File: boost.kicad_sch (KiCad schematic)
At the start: 24 parts, among them Q13 BSC059N04LS6, Q8 BSC059N04LS6, U7 LM5123-Q1

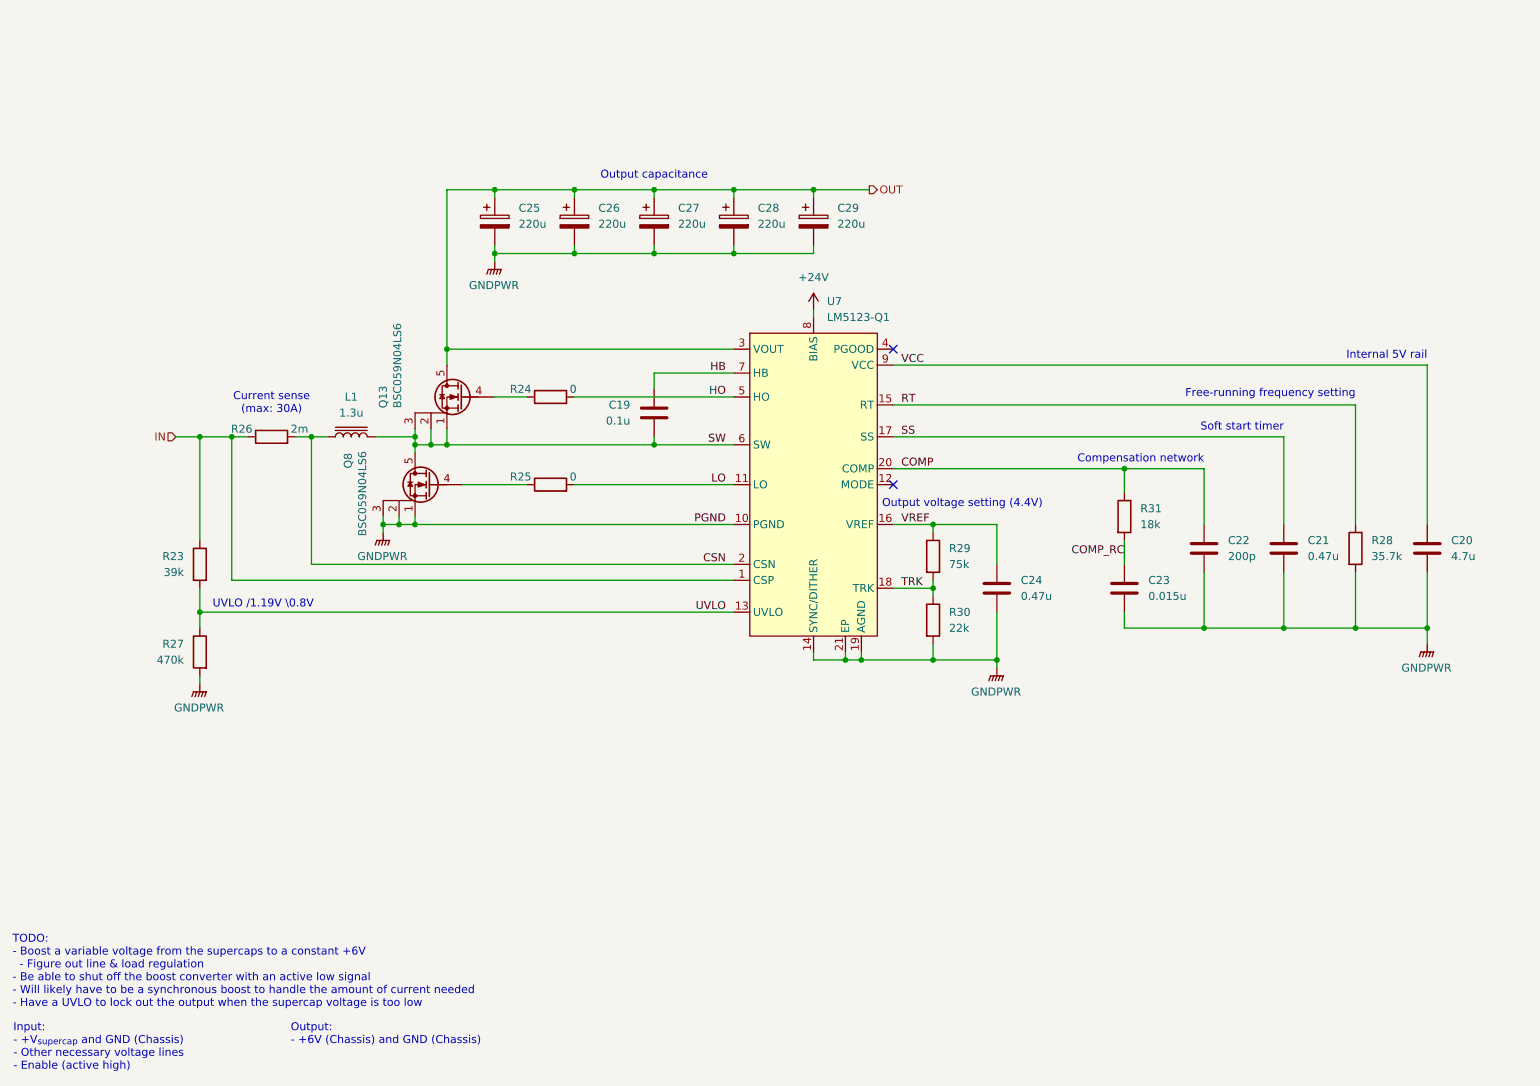
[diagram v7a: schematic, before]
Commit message: Reannotate schematic
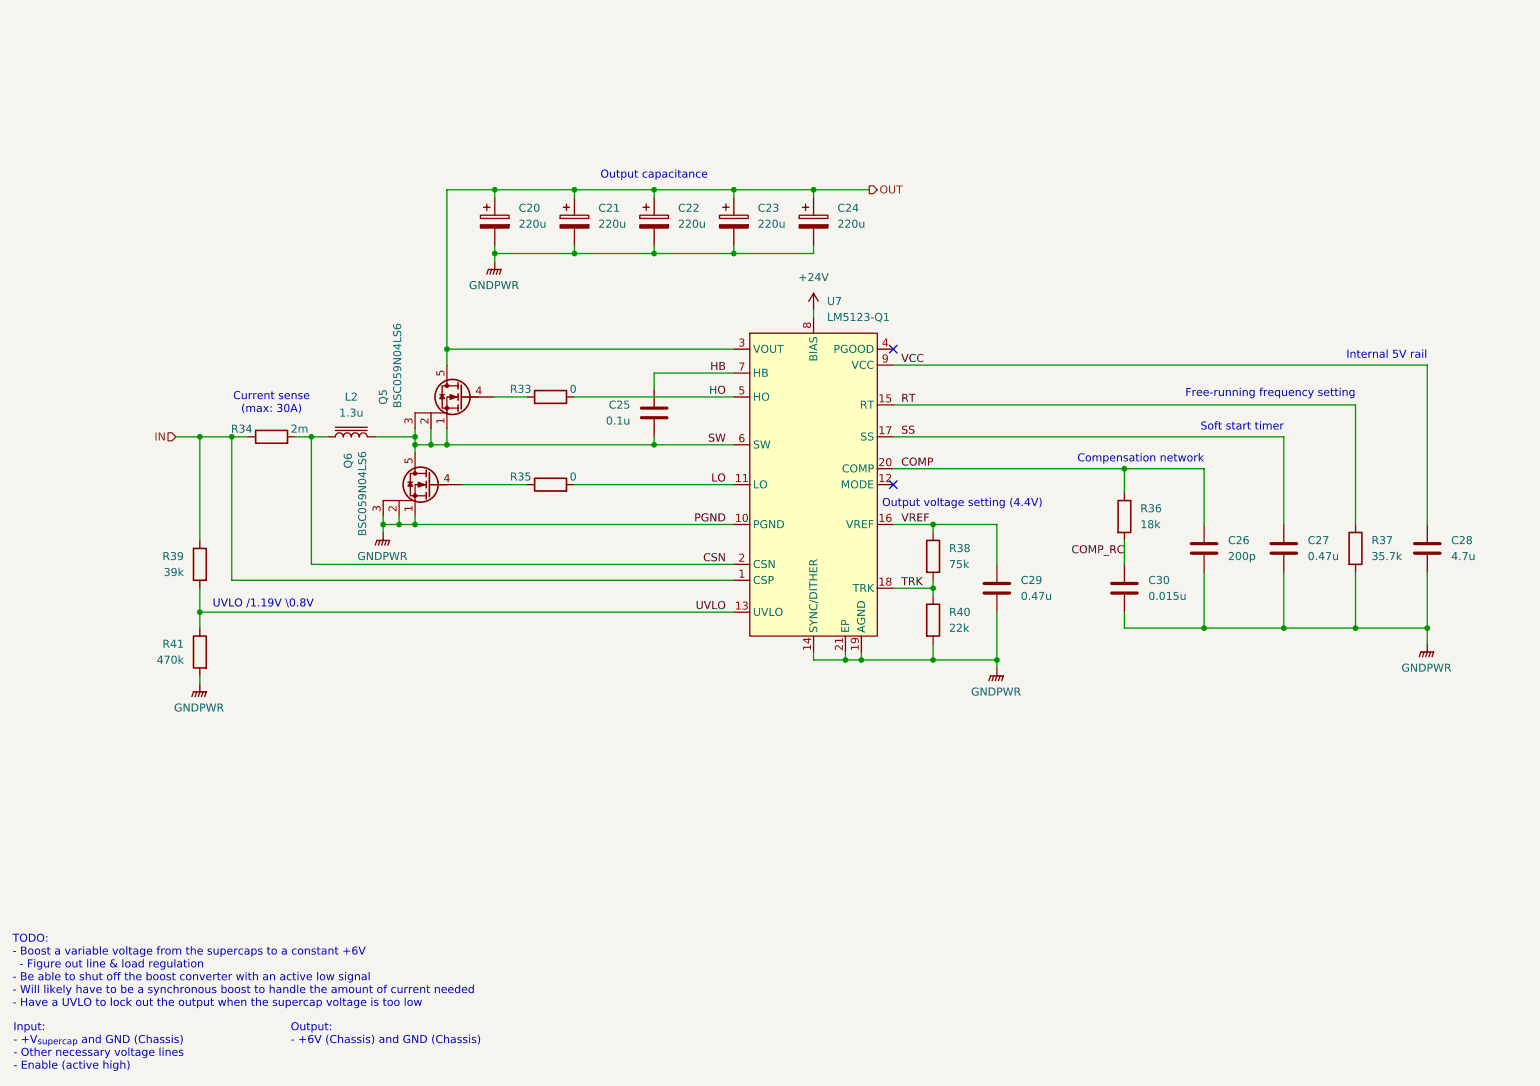
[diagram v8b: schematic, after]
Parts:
- renumbered C25 to C20, C26 to C21, C27 to C22, C28 to C23, C29 to C24, C19 to C25, C22 to C26, C21 to C27, C20 to C28, C24 to C29, C23 to C30, L1 to L2, Q13 to Q5, Q8 to Q6, R24 to R33, R26 to R34, R25 to R35, R31 to R36, R28 to R37, R29 to R38, R23 to R39, R30 to R40, R27 to R41
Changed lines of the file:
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@@
 		(on_board yes)
 		(dnp no)
-		(property "Reference" "Q13"
+		(property "Reference" "Q5"
 			(at 78.74 83.82 90)
 			(effects
@@
 			(project "SupercapManager"
 				(path "/6197145b-e7d4-44cc-9d90-537b6501bf60/fd749e99-bd1e-4aca-86d6-8b572dc00b7d"
-					(reference "Q13")
+					(reference "Q5")
 					(unit 1)
 				)
@@
 		(on_board yes)
 		(dnp no)
-		(property "Reference" "R27"
+		(property "Reference" "R41"
 			(at 46.99 123.1899 0)
 			(effects
@@
 			(project "SupercapManager"
 				(path "/6197145b-e7d4-44cc-9d90-537b6501bf60/fd749e99-bd1e-4aca-86d6-8b572dc00b7d"
-					(reference "R27")
+					(reference "R41")
 					(unit 1)
 				)
@@
 		(dnp no)
 		(fields_autoplaced yes)
-		(property "Reference" "C27"
+		(property "Reference" "C22"
 			(at 125.73 53.7209 0)
 			(effects
@@
 			(project "SupercapManager"
 				(path "/6197145b-e7d4-44cc-9d90-537b6501bf60/fd749e99-bd1e-4aca-86d6-8b572dc00b7d"
-					(reference "C27")
+					(reference "C22")
 					(unit 1)
 				)
@@
 		(dnp no)
 		(fields_autoplaced yes)
-		(property "Reference" "#PWR046"
+		(property "Reference" "#PWR050"
 			(at 245.11 128.27 0)
 			(effects
@@
 			(project "SupercapManager"
 				(path "/6197145b-e7d4-44cc-9d90-537b6501bf60/fd749e99-bd1e-4aca-86d6-8b572dc00b7d"
-					(reference "#PWR046")
+					(reference "#PWR050")
 					(unit 1)
 				)
@@
 		(on_board yes)
 		(dnp no)
-		(property "Reference" "C20"
+		(property "Reference" "C28"
 			(at 248.92 106.6799 0)
 			(effects
@@
 			(project "SupercapManager"
 				(path "/6197145b-e7d4-44cc-9d90-537b6501bf60/fd749e99-bd1e-4aca-86d6-8b572dc00b7d"
-					(reference "C20")
+					(reference "C28")
 					(unit 1)
 				)
@@
 		(dnp no)
 		(fields_autoplaced yes)
-		(property "Reference" "C25"
+		(property "Reference" "C20"
 			(at 100.33 53.7209 0)
 			(effects
@@
 			(project ""
 				(path "/6197145b-e7d4-44cc-9d90-537b6501bf60/fd749e99-bd1e-4aca-86d6-8b572dc00b7d"
-					(reference "C25")
+					(reference "C20")
 					(unit 1)
 				)
@@
 		(dnp no)
 		(fields_autoplaced yes)
-		(property "Reference" "#PWR020"
+		(property "Reference" "#PWR051"
 			(at 176.53 132.08 0)
 			(effects
@@
 			(project ""
 				(path "/6197145b-e7d4-44cc-9d90-537b6501bf60/fd749e99-bd1e-4aca-86d6-8b572dc00b7d"
-					(reference "#PWR020")
+					(reference "#PWR051")
 					(unit 1)
 				)
@@
 		(on_board yes)
 		(dnp no)
-		(property "Reference" "R28"
+		(property "Reference" "R37"
 			(at 236.22 106.6799 0)
 			(effects
@@
 			(project "SupercapManager"
 				(path "/6197145b-e7d4-44cc-9d90-537b6501bf60/fd749e99-bd1e-4aca-86d6-8b572dc00b7d"
-					(reference "R28")
+					(reference "R37")
 					(unit 1)
 				)
@@
 		(on_board yes)
 		(dnp no)
-		(property "Reference" "C22"
+		(property "Reference" "C26"
 			(at 213.36 106.6799 0)
 			(effects
@@
 			(project "SupercapManager"
 				(path "/6197145b-e7d4-44cc-9d90-537b6501bf60/fd749e99-bd1e-4aca-86d6-8b572dc00b7d"
-					(reference "C22")
+					(reference "C26")
 					(unit 1)
 				)
@@
 		(on_board yes)
 		(dnp no)
-		(property "Reference" "R23"
+		(property "Reference" "R39"
 			(at 46.99 109.2199 0)
 			(effects
@@
 			(project ""
 				(path "/6197145b-e7d4-44cc-9d90-537b6501bf60/fd749e99-bd1e-4aca-86d6-8b572dc00b7d"
-					(reference "R23")
+					(reference "R39")
 					(unit 1)
 				)
@@
 		(on_board yes)
 		(dnp no)
-		(property "Reference" "R24"
+		(property "Reference" "R33"
 			(at 102.362 83.312 90)
 			(effects
@@
 			(project "SupercapManager"
 				(path "/6197145b-e7d4-44cc-9d90-537b6501bf60/fd749e99-bd1e-4aca-86d6-8b572dc00b7d"
-					(reference "R24")
+					(reference "R33")
 					(unit 1)
 				)
@@
 		(on_board yes)
 		(dnp no)
-		(property "Reference" "R25"
+		(property "Reference" "R35"
 			(at 102.362 97.282 90)
 			(effects
@@
 			(project "SupercapManager"
 				(path "/6197145b-e7d4-44cc-9d90-537b6501bf60/fd749e99-bd1e-4aca-86d6-8b572dc00b7d"
-					(reference "R25")
+					(reference "R35")
 					(unit 1)
 				)
@@
 		(dnp no)
 		(fields_autoplaced yes)
-		(property "Reference" "C29"
+		(property "Reference" "C24"
 			(at 151.13 53.7209 0)
 			(effects
@@
 			(project "SupercapManager"
 				(path "/6197145b-e7d4-44cc-9d90-537b6501bf60/fd749e99-bd1e-4aca-86d6-8b572dc00b7d"
-					(reference "C29")
+					(reference "C24")
 					(unit 1)
 				)
@@
 		(on_board yes)
 		(dnp no)
-		(property "Reference" "R26"
+		(property "Reference" "R34"
 			(at 57.912 89.662 90)
 			(effects
@@
 			(project "SupercapManager"
 				(path "/6197145b-e7d4-44cc-9d90-537b6501bf60/fd749e99-bd1e-4aca-86d6-8b572dc00b7d"
-					(reference "R26")
+					(reference "R34")
 					(unit 1)
 				)
@@
 		(on_board yes)
 		(dnp no)
-		(property "Reference" "C21"
+		(property "Reference" "C27"
 			(at 226.06 106.6799 0)
 			(effects
@@
 			(project "SupercapManager"
 				(path "/6197145b-e7d4-44cc-9d90-537b6501bf60/fd749e99-bd1e-4aca-86d6-8b572dc00b7d"
-					(reference "C21")
+					(reference "C27")
 					(unit 1)
 				)
@@
 		(on_board yes)
 		(dnp no)
-		(property "Reference" "C23"
+		(property "Reference" "C30"
 			(at 200.66 113.0299 0)
 			(effects
@@
 			(project "SupercapManager"
 				(path "/6197145b-e7d4-44cc-9d90-537b6501bf60/fd749e99-bd1e-4aca-86d6-8b572dc00b7d"
-					(reference "C23")
+					(reference "C30")
 					(unit 1)
 				)
@@
 		(on_board yes)
 		(dnp no)
-		(property "Reference" "R30"
+		(property "Reference" "R40"
 			(at 168.91 118.1099 0)
 			(effects
@@
 			(project "SupercapManager"
 				(path "/6197145b-e7d4-44cc-9d90-537b6501bf60/fd749e99-bd1e-4aca-86d6-8b572dc00b7d"
-					(reference "R30")
+					(reference "R40")
 					(unit 1)
 				)
@@
 		(dnp no)
 		(fields_autoplaced yes)
-		(property "Reference" "C26"
+		(property "Reference" "C21"
 			(at 113.03 53.7209 0)
 			(effects
@@
 			(project "SupercapManager"
 				(path "/6197145b-e7d4-44cc-9d90-537b6501bf60/fd749e99-bd1e-4aca-86d6-8b572dc00b7d"
-					(reference "C26")
+					(reference "C21")
 					(unit 1)
 				)
@@
 		(on_board yes)
 		(dnp no)
-		(property "Reference" "R31"
+		(property "Reference" "R36"
 			(at 199.39 101.5999 0)
 			(effects
@@
 			(project "SupercapManager"
 				(path "/6197145b-e7d4-44cc-9d90-537b6501bf60/fd749e99-bd1e-4aca-86d6-8b572dc00b7d"
-					(reference "R31")
+					(reference "R36")
 					(unit 1)
 				)
@@
 		(on_board yes)
 		(dnp no)
-		(property "Reference" "Q8"
+		(property "Reference" "Q6"
 			(at 73.152 93.98 90)
 			(effects
@@
 			(project "SupercapManager"
 				(path "/6197145b-e7d4-44cc-9d90-537b6501bf60/fd749e99-bd1e-4aca-86d6-8b572dc00b7d"
-					(reference "Q8")
+					(reference "Q6")
 					(unit 1)
 				)
@@
 		(dnp no)
 		(fields_autoplaced yes)
-		(property "Reference" "#PWR043"
+		(property "Reference" "#PWR049"
 			(at 78.74 110.49 0)
 			(effects
@@
 			(project "SupercapManager"
 				(path "/6197145b-e7d4-44cc-9d90-537b6501bf60/fd749e99-bd1e-4aca-86d6-8b572dc00b7d"
-					(reference "#PWR043")
+					(reference "#PWR049")
 					(unit 1)
 				)
@@
 		(on_board yes)
 		(dnp no)
-		(property "Reference" "C24"
+		(property "Reference" "C29"
 			(at 180.34 113.0299 0)
 			(effects
@@
 			(project "SupercapManager"
 				(path "/6197145b-e7d4-44cc-9d90-537b6501bf60/fd749e99-bd1e-4aca-86d6-8b572dc00b7d"
-					(reference "C24")
+					(reference "C29")
 					(unit 1)
 				)
@@
 		(on_board yes)
 		(dnp no)
-		(property "Reference" "C19"
+		(property "Reference" "C25"
 			(at 118.11 85.0899 0)
 			(effects
@@
 			(project ""
 				(path "/6197145b-e7d4-44cc-9d90-537b6501bf60/fd749e99-bd1e-4aca-86d6-8b572dc00b7d"
-					(reference "C19")
+					(reference "C25")
 					(unit 1)
 				)
@@
 		(dnp no)
 		(fields_autoplaced yes)
-		(property "Reference" "L1"
+		(property "Reference" "L2"
 			(at 73.66 83.82 90)
 			(effects
@@
 			(project ""
 				(path "/6197145b-e7d4-44cc-9d90-537b6501bf60/fd749e99-bd1e-4aca-86d6-8b572dc00b7d"
-					(reference "L1")
+					(reference "L2")
 					(unit 1)
 				)
@@
 		(dnp no)
 		(fields_autoplaced yes)
-		(property "Reference" "#PWR044"
+		(property "Reference" "#PWR052"
 			(at 49.53 134.62 0)
 			(effects
@@
 			(project "SupercapManager"
 				(path "/6197145b-e7d4-44cc-9d90-537b6501bf60/fd749e99-bd1e-4aca-86d6-8b572dc00b7d"
-					(reference "#PWR044")
+					(reference "#PWR052")
 					(unit 1)
 				)
@@
 		(on_board yes)
 		(dnp no)
-		(property "Reference" "R29"
+		(property "Reference" "R38"
 			(at 168.91 107.9499 0)
 			(effects
@@
 			(project "SupercapManager"
 				(path "/6197145b-e7d4-44cc-9d90-537b6501bf60/fd749e99-bd1e-4aca-86d6-8b572dc00b7d"
-					(reference "R29")
+					(reference "R38")
 					(unit 1)
 				)
@@
 		(dnp no)
 		(fields_autoplaced yes)
-		(property "Reference" "#PWR045"
+		(property "Reference" "#PWR048"
 			(at 147.32 73.66 0)
 			(effects
@@
 			(project ""
 				(path "/6197145b-e7d4-44cc-9d90-537b6501bf60/fd749e99-bd1e-4aca-86d6-8b572dc00b7d"
-					(reference "#PWR045")
+					(reference "#PWR048")
 					(unit 1)
 				)
@@
 		(dnp no)
 		(fields_autoplaced yes)
-		(property "Reference" "C28"
+		(property "Reference" "C23"
 			(at 138.43 53.7209 0)
 			(effects
@@
 			(project "SupercapManager"
 				(path "/6197145b-e7d4-44cc-9d90-537b6501bf60/fd749e99-bd1e-4aca-86d6-8b572dc00b7d"
-					(reference "C28")
-					(unit 1)
-				)
+					(reference "C23")
+					(unit 1)
+				)
